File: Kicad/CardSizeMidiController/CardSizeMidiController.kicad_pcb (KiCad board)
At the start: 2 copper layers, 85.7 x 54 mm, 41 parts, among them J1 USB_B, J2 Conn_02x03_Odd_Even, J3 MIDI OUT, J4 AudioJack3, J5 Screw_Terminal_01x01, J6 Screw_Terminal_01x01, J7 Screw_Terminal_01x01, J8 Screw_Terminal_01x01, SW0 SW_Push, SW1 SW_Push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

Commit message: small layout changes
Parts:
- J4: footprint SensaiLib:Jack stereo tayda -> SensaiLib:Jack stereo tayda no extra holes
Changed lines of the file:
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@@
     (add_net GND)
+  )
+  (module "SensaiLib:Jack stereo tayda no extra holes" (layer F.Cu)
+    (at 68.707 6.477 180)
+    (fp_text reference J4 (at 0 -10 180) (layer F.SilkS)
+      (effects (font (size 1 1) (thickness 0.15)))
+    )
+    (fp_text value AudioJack3 (at 0 -8.5 180) (layer F.Fab)
+      (effects (font (size 1 1) (thickness 0.15)))
+    )
+    (fp_line (start -4.5 3.5) (end -4.5 4.5) (layer F.SilkS) (width 0.15))
+    (fp_line (start 3 4.5) (end 3 6.5) (layer F.SilkS) (width 0.15))
+    (fp_line (start 6 3.5) (end 4.5 3.5) (layer F.SilkS) (width 0.15))
+    (fp_line (start -4.5 3.5) (end -6 3.5) (layer F.SilkS) (width 0.15))
+    (fp_line (start 4.5 4.5) (end -4.5 4.5) (layer F.SilkS) (width 0.15))
+    (fp_line (start 6 -7.5) (end 6 3.5) (layer F.SilkS) (width 0.15))
+    (fp_line (start -2.95 4.5) (end -2.95 6.5) (layer F.SilkS) (width 0.15))
+    (fp_line (start 4.5 3.5) (end 4.5 4.5) (layer F.SilkS) (width 0.15))
+    (fp_line (start 3 6.5) (end -2.95 6.5) (layer F.SilkS) (width 0.15))
+    (fp_line (start -2.9 5.5) (end 3 5.5) (layer F.SilkS) (width 0.15))
+    (fp_line (start -6 3.5) (end -6 -7.5) (layer F.SilkS) (width 0.15))
+    (fp_line (start -6 -7.5) (end 6 -7.5) (layer F.SilkS) (width 0.15))
+    (pad S thru_hole roundrect (at 0 0 180) (size 2.4 1.6) (drill oval 1.6 0.7) (layers *.Cu *.Mask) (roundrect_rratio 0.25)
+      (net 1 GND))
+    (pad TN thru_hole roundrect (at 2.5 -5 180) (size 1.6 2.4) (drill oval 0.7 1.6) (layers *.Cu *.Mask) (roundrect_rratio 0.25))
+    (pad RN thru_hole roundrect (at -2.5 -5 180) (size 1.6 2.4) (drill oval 0.7 1.6) (layers *.Cu *.Mask) (roundrect_rratio 0.25))
+    (pad T thru_hole roundrect (at 5 -5 180) (size 1.6 2.4) (drill oval 0.7 1.6) (layers *.Cu *.Mask) (roundrect_rratio 0.25)
+      (net 38 "Net-(J3-Pad5)"))
+    (pad R thru_hole roundrect (at -5 -5 180) (size 1.6 2.4) (drill oval 0.7 1.6) (layers *.Cu *.Mask) (roundrect_rratio 0.25)
+      (net 36 "Net-(J3-Pad4)"))
   )
   (module Button_Switch_THT:SW_PUSH_6mm_H5mm (layer F.Cu)
@@
     )
   )
-  (module "SensaiLib:Jack stereo tayda" (layer F.Cu)
-    (at 68.707 6.477 180)
-    (fp_text reference J4 (at 0 -2.794 180) (layer F.SilkS)
-      (effects (font (size 1 1) (thickness 0.15)))
-    )
-    (fp_text value AudioJack3 (at -0.2 -10.8 180) (layer F.Fab)
-      (effects (font (size 1 1) (thickness 0.15)))
-    )
-    (fp_line (start -6 -7.5) (end 6 -7.5) (layer F.SilkS) (width 0.15))
-    (fp_line (start 6 -7.5) (end 6 3.5) (layer F.SilkS) (width 0.15))
-    (fp_line (start 4.5 4.5) (end -4.5 4.5) (layer F.SilkS) (width 0.15))
-    (fp_line (start -6 3.5) (end -6 -7.5) (layer F.SilkS) (width 0.15))
-    (fp_line (start 3 4.5) (end 3 6.5) (layer F.SilkS) (width 0.15))
-    (fp_line (start 3 6.5) (end -2.95 6.5) (layer F.SilkS) (width 0.15))
-    (fp_line (start -2.95 4.5) (end -2.95 6.5) (layer F.SilkS) (width 0.15))
-    (fp_line (start -4.5 3.5) (end -4.5 4.5) (layer F.SilkS) (width 0.15))
-    (fp_line (start 4.5 3.5) (end 4.5 4.5) (layer F.SilkS) (width 0.15))
-    (fp_line (start -4.5 3.5) (end -6 3.5) (layer F.SilkS) (width 0.15))
-    (fp_line (start 6 3.5) (end 4.5 3.5) (layer F.SilkS) (width 0.15))
-    (fp_line (start -2.9 5.5) (end 3 5.5) (layer F.SilkS) (width 0.15))
-    (pad R thru_hole roundrect (at -5 -5 180) (size 1.6 2.4) (drill oval 0.7 1.6) (layers *.Cu *.Mask) (roundrect_rratio 0.25)
-      (net 36 "Net-(J3-Pad4)"))
-    (pad T thru_hole roundrect (at 5 -5 180) (size 1.6 2.4) (drill oval 0.7 1.6) (layers *.Cu *.Mask) (roundrect_rratio 0.25)
-      (net 38 "Net-(J3-Pad5)"))
-    (pad RN thru_hole roundrect (at -2.5 -5 180) (size 1.6 2.4) (drill oval 0.7 1.6) (layers *.Cu *.Mask) (roundrect_rratio 0.25))
-    (pad TN thru_hole roundrect (at 2.5 -5 180) (size 1.6 2.4) (drill oval 0.7 1.6) (layers *.Cu *.Mask) (roundrect_rratio 0.25))
-    (pad S thru_hole roundrect (at 0 0 180) (size 2.4 1.6) (drill oval 1.6 0.7) (layers *.Cu *.Mask) (roundrect_rratio 0.25)
-      (net 1 GND))
-  )
   (module SensaiLib:din-5 (layer F.Cu)

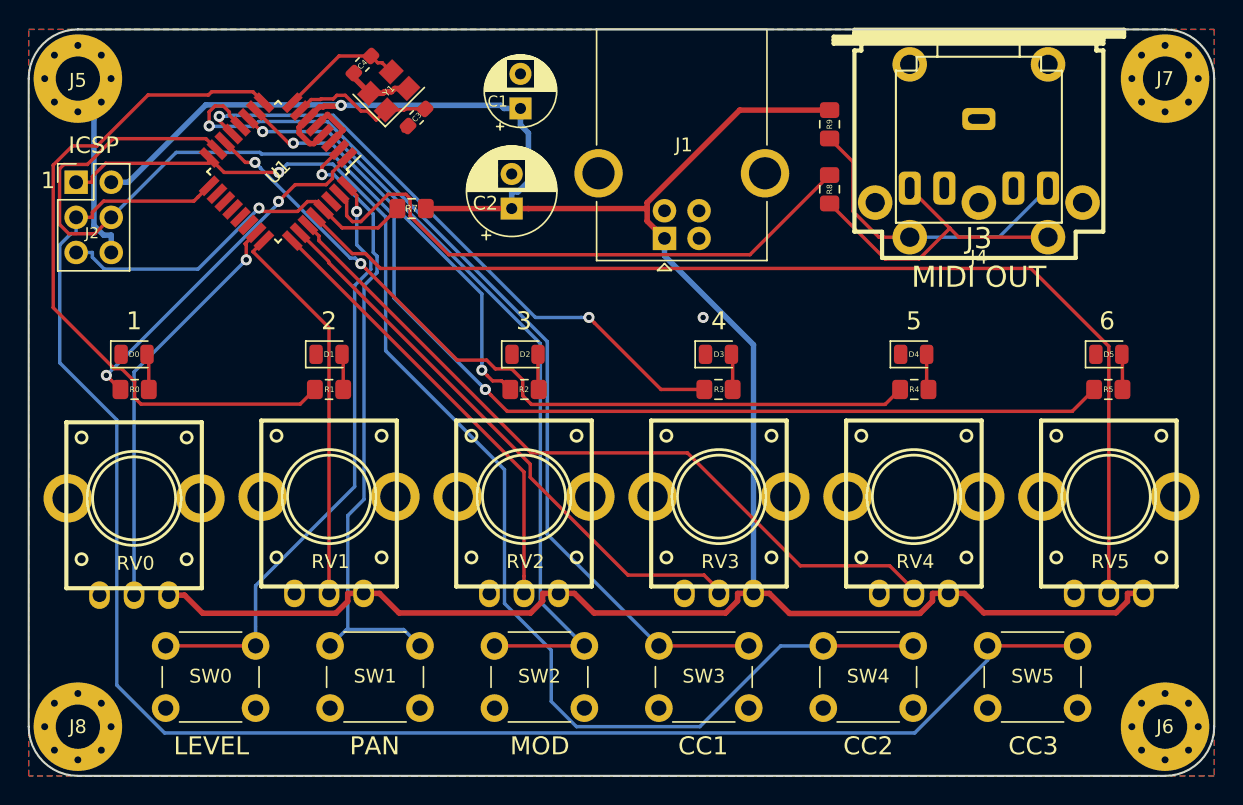
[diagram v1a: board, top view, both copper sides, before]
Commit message: new silkscreen design, created logo and labels, minor layout changes
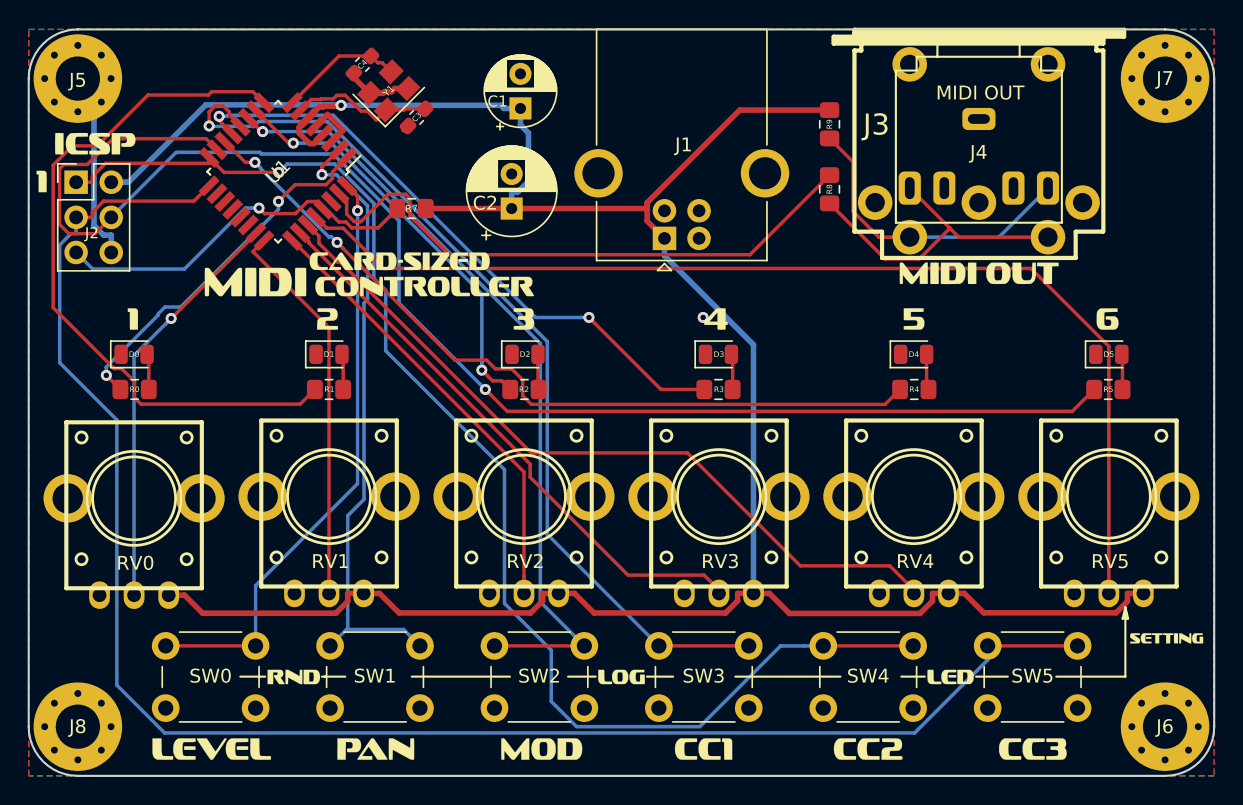
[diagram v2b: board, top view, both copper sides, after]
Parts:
- added LOGO1: Logo_Open_Hardware_Small, Card sized midi controller Silckscreen:card sized midi controller logo, F.Cu at (24.6, 18.3)
- added LOGO10: Logo_Open_Hardware_Small, Card sized midi controller Silckscreen:3, F.Cu at (35.9, 21.0)
- added LOGO11: Logo_Open_Hardware_Small, Card sized midi controller Silckscreen:4, F.Cu at (49.9, 21.0)
- added LOGO12: Logo_Open_Hardware_Small, Card sized midi controller Silckscreen:5, F.Cu at (64.2, 20.9)
- added LOGO13: Logo_Open_Hardware_Small, Card sized midi controller Silckscreen:6, F.Cu at (78.2, 21.0)
- added LOGO14: Logo_Open_Hardware_Small, Card sized midi controller Silckscreen:1, F.Cu at (1.30, 11.1)
- added LOGO15: Logo_Open_Hardware_Small, Card sized midi controller Silckscreen:level, F.Cu at (17.0, 50.5)
- added LOGO16: Logo_Open_Hardware_Small, Card sized midi controller Silckscreen:pan, F.Cu at (28.9, 50.5)
- added LOGO17: Logo_Open_Hardware_Small, Card sized midi controller Silckscreen:mod, F.Cu at (40.9, 50.5)
- added LOGO18: Logo_Open_Hardware_Small, Card sized midi controller Silckscreen:cc1, F.Cu at (52.6, 50.5)
- added LOGO19: Logo_Open_Hardware_Small, Card sized midi controller Silckscreen:cc2, F.Cu at (64.5, 50.5)
- added LOGO2: Logo_Open_Hardware_Small, Card sized midi controller Silckscreen:ICSP, F.Cu at (4.50, 8.30)
- added LOGO20: Logo_Open_Hardware_Small, Card sized midi controller Silckscreen:cc3, F.Cu at (76.4, 50.5)
- added LOGO3: Logo_Open_Hardware_Small, Card sized midi controller Silckscreen:midi out, F.Cu at (72.5, 16.1)
- added LOGO4: Logo_Open_Hardware_Small, Card sized midi controller Silckscreen:setting, F.Cu at (84.1, 43.3)
- added LOGO5: Logo_Open_Hardware_Small, Card sized midi controller Silckscreen:rnd, F.Cu at (21.7, 45.8)
- added LOGO6: Logo_Open_Hardware_Small, Card sized midi controller Silckscreen:log, F.Cu at (45.4, 45.8)
- added LOGO7: Logo_Open_Hardware_Small, Card sized midi controller Silckscreen:led, F.Cu at (69.2, 45.8)
- added LOGO8: Logo_Open_Hardware_Small, Card sized midi controller Silckscreen:1, F.Cu at (7.90, 21.0)
- added LOGO9: Logo_Open_Hardware_Small, Card sized midi controller Silckscreen:2, F.Cu at (21.8, 21.1)
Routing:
- net SW0: track 43.9 -> 43.1 mm
- net LED0: track 25.7 -> 26.4 mm
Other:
- board text added: "Version 0.3"
- board text removed: "1"
- board text removed: "2"
- board text removed: "3"
- board text removed: "4"
- board text removed: "5"
- board text removed: "6"
- board text removed: "CC1"
- board text removed: "CC2"
- board text removed: "CC3"
- board text removed: "ICSP"
- board text removed: "LEVEL"
- board text removed: "MOD"
- board text removed: "PAN"
- board text removed: "Version 0.2"
